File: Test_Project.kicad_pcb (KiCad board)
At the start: 4 copper layers, 72.5 x 56.2 mm, 72 parts, among them J1 Conn_01x02, J2 Conn_01x02, J3 Conn_01x03, J4 Conn_01x04, J5 Conn_01x04, J6 Conn_01x04, J7 Conn_01x04, Q1 NTTFS5C454NLTAG, Q2 NTTFS5C454NLTAG, Q3 NTTFS5C454NLTAG, Q4 NTTFS5C454NLTAG, Q5 BSS138-7-F, U1 STM32L081KZTx, U2 MIC2132YML, U3 AP2127N-3.3TRG1

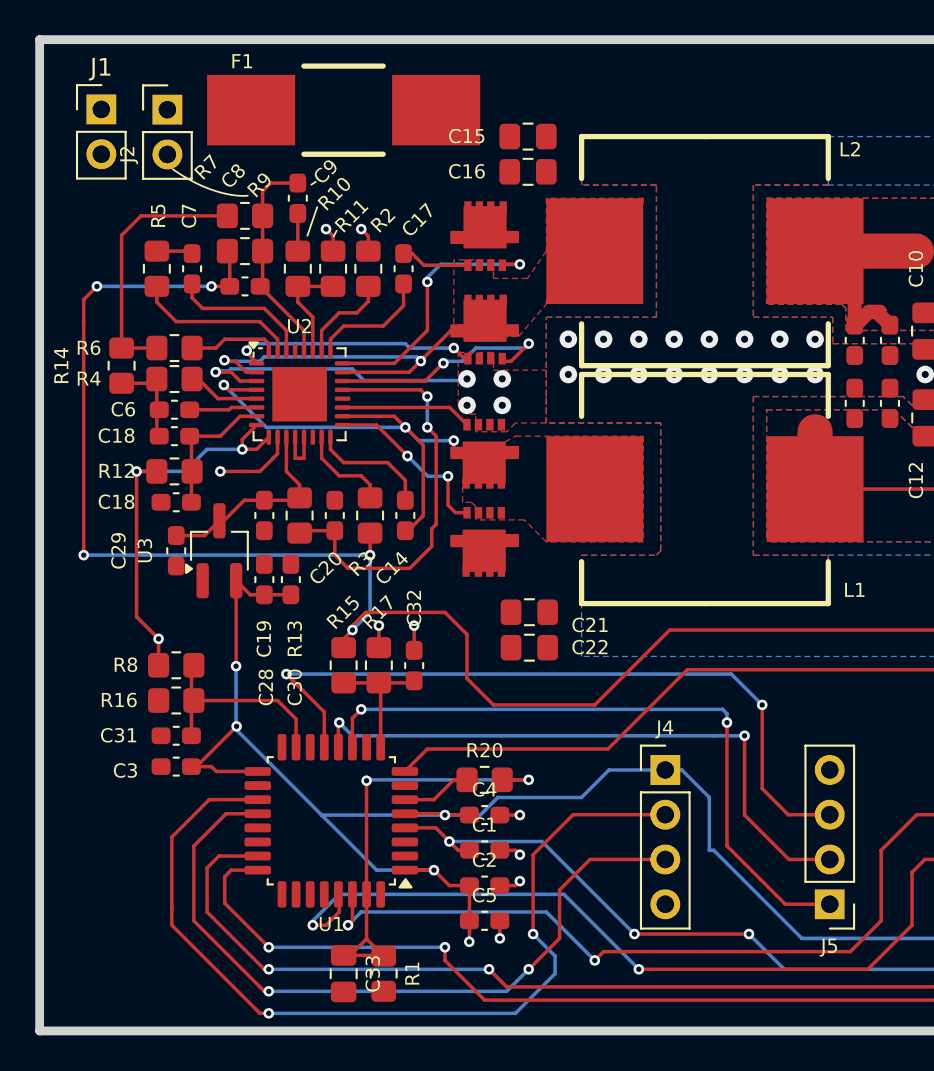
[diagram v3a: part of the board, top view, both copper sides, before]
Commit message: Finished up routing nets and pouring polygons. Needs final ground pours and review before ordering.
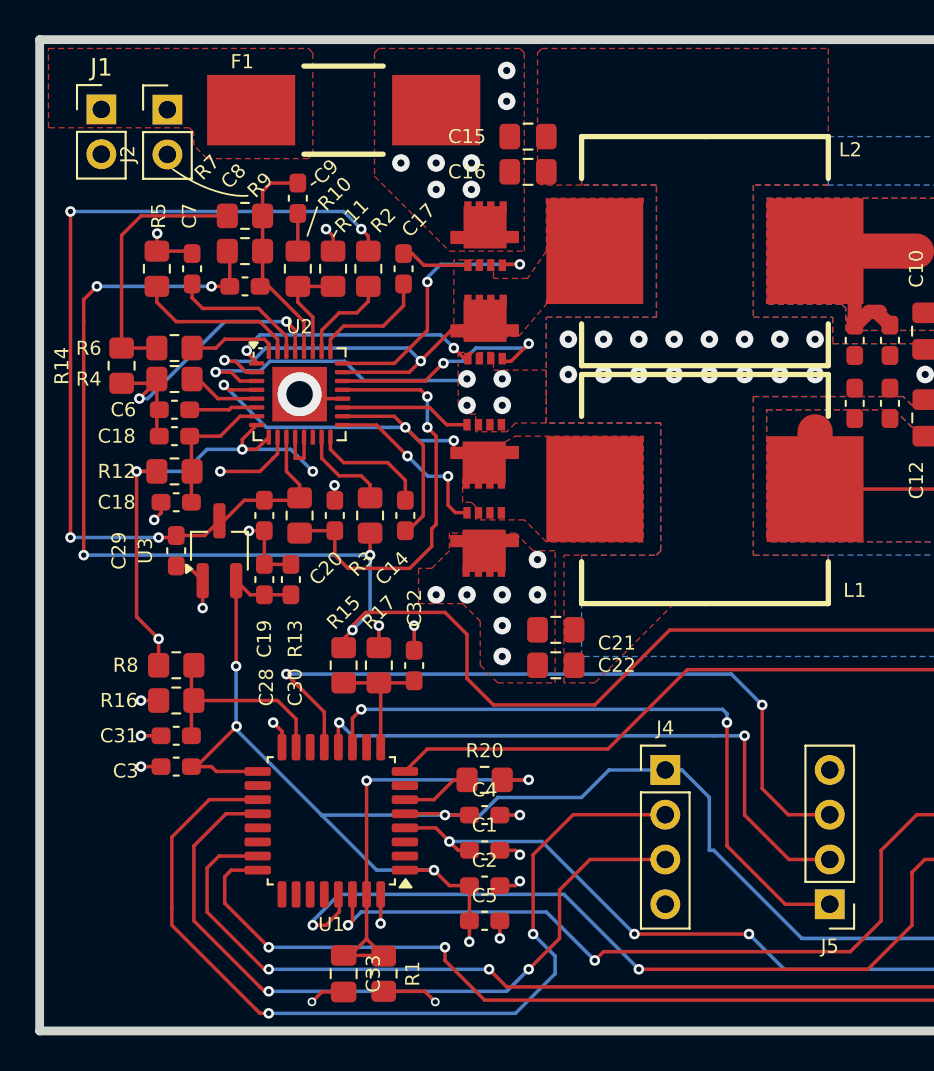
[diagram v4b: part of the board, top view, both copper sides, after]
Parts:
- moved C21 1.80 mm to (360.0, 104.5)
- moved C22 1.80 mm to (360.0, 106.5)
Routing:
- net GND: track 52.1 -> 100.3 mm, vias 33 -> 48
- net /VDD_5V: track 13.1 -> 54.5 mm, vias 1 -> 4
- net /Vin: track 22.7 -> 27.2 mm, vias 3 -> 18
- added copper zone on F.Cu, net /12V
- added copper zone on F.Cu, net /Vin
- added copper zone on In2.Cu, net /Vin
- added copper zone on In2.Cu, net /Vout

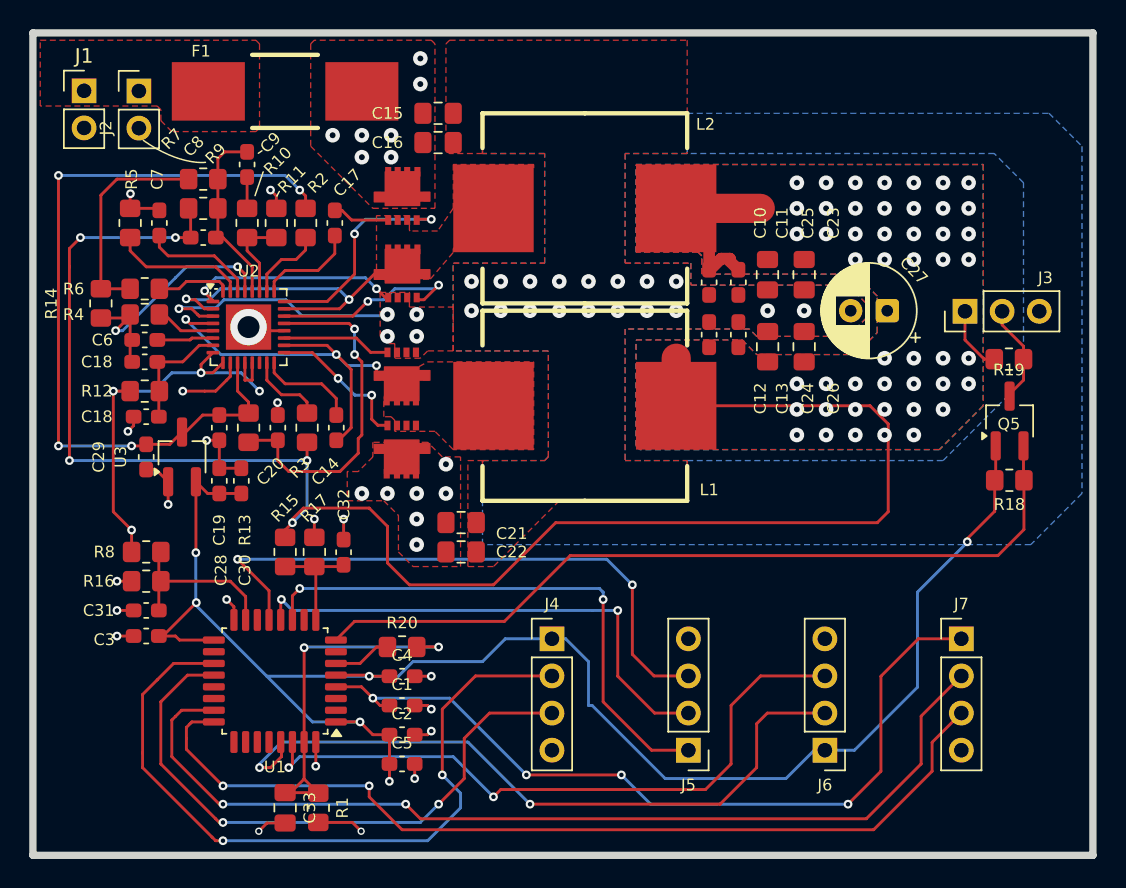
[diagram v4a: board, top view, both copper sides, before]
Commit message: Finished up layout and added some mounting holes.
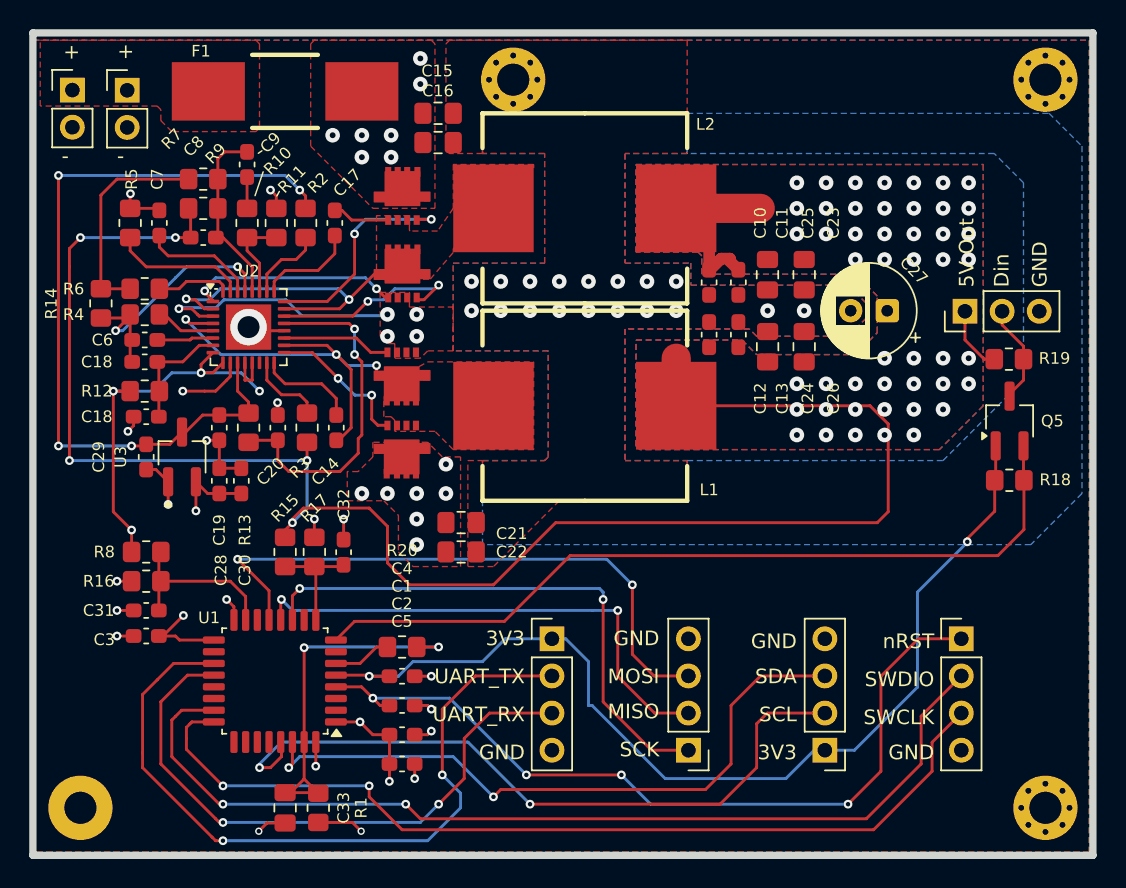
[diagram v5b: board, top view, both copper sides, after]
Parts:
- added ?: , Test_Project_Lib:, F.Cu at (334.0, 124.0)
- added ?: MountingHole_2.2mm_M2_Pad_Via, Test_Project_Lib:MountingHole_2.2mm_M2_Pad_Via, F.Cu at (363.6, 74.2)
- added ?: MountingHole_2.2mm_M2_Pad_Via, Test_Project_Lib:MountingHole_2.2mm_M2_Pad_Via, F.Cu at (400.0, 74.2)
- added ?: MountingHole_2.2mm_M2_Pad_Via, Test_Project_Lib:MountingHole_2.2mm_M2_Pad_Via, F.Cu at (400.0, 124.0)
- added G***: LOGO, Test_Project_Lib:LOGO, B.Cu at (369.6, 99.3)
- moved J1 0.80 mm to (333.4, 74.9)
- moved J2 0.80 mm to (337.2, 74.9)
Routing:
- net /VDD_3V3: track 117.3 -> 88.1 mm
- added copper zone on In2.Cu, net /12V
- added copper zone on In2.Cu, net /VDD_3V3
- added copper zone on In2.Cu, net /VDD_5V
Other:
- board text added: "+"
- board text added: "-"
- board text added: "3V3"
- board text added: "5V Out"
- board text added: "Din"
- board text added: "GND"
- board text added: "MISO"
- board text added: "MOSI"
- board text added: "SCK"
- board text added: "SCL"
- board text added: "SDA"
- board text added: "SWCLK"
- board text added: "SWDIO"
- board text added: "UART_RX"
- board text added: "UART_TX"
- board text added: "nRST"

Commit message: Daily commit. Working through test points and DRC checks.
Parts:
- removed the ? at (334.0, 124.0)
- added ?: , , F.Cu at (335.6, 125.0)
- added ?: , , F.Cu at (334.4, 125.5)
- added ?: , , F.Cu at (380.0, 97.2)
- added ?: , , F.Cu at (333.6, 86.8)
- added ?: , , F.Cu at (380.0, 82.0)
- added ?: , , F.Cu at (333.2, 125.0)
- added ?: , , F.Cu at (335.6, 122.6)
- added ?: , , F.Cu at (336.1, 123.8)
- added ?: , , F.Cu at (332.5, 84.1)
- added ?: , , F.Cu at (334.4, 122.2)
- added ?: , , F.Cu at (380.0, 102.2)
- added ?: , , F.Cu at (333.2, 122.6)
- added ?: , , F.Cu at (380.0, 77.0)
- added ?: , , F.Cu at (334.2, 123.8)
- added ?: , , F.Cu at (397.8, 83.8)
- added ?: , , F.Cu at (332.8, 123.8)
- C1: renamed from C7; footprint Test_Project_Lib:C_0603_1608Metric_Pad1.08x0.95mm_HandSolder -> Capacitor_SMD:C_0603_1608Metric_Pad1.08x0.95mm_HandSolder
- C10: renamed from C23; footprint Test_Project_Lib:C_0805_2012Metric_Pad1.18x1.45mm_HandSolder -> Capacitor_SMD:C_0805_2012Metric_Pad1.18x1.45mm_HandSolder
- C11: renamed from C6; footprint Test_Project_Lib:C_0603_1608Metric_Pad1.08x0.95mm_HandSolder -> Capacitor_SMD:C_0603_1608Metric_Pad1.08x0.95mm_HandSolder
- C12: renamed from C18; footprint Test_Project_Lib:C_0603_1608Metric_Pad1.08x0.95mm_HandSolder -> Capacitor_SMD:C_0603_1608Metric_Pad1.08x0.95mm_HandSolder
- C13: renamed from C29; footprint Test_Project_Lib:C_0603_1608Metric_Pad1.08x0.95mm_HandSolder -> Capacitor_SMD:C_0603_1608Metric_Pad1.08x0.95mm_HandSolder
- C14: renamed from C3; footprint Test_Project_Lib:C_0603_1608Metric_Pad1.08x0.95mm_HandSolder -> Capacitor_SMD:C_0603_1608Metric_Pad1.08x0.95mm_HandSolder
- C16: renamed from C31; footprint Test_Project_Lib:C_0603_1608Metric_Pad1.08x0.95mm_HandSolder -> Capacitor_SMD:C_0603_1608Metric_Pad1.08x0.95mm_HandSolder
- C17: renamed from C22; footprint Test_Project_Lib:C_0805_2012Metric_Pad1.18x1.45mm_HandSolder -> Capacitor_SMD:C_0805_2012Metric_Pad1.18x1.45mm_HandSolder
- C18: renamed from C21; footprint Test_Project_Lib:C_0805_2012Metric_Pad1.18x1.45mm_HandSolder -> Capacitor_SMD:C_0805_2012Metric_Pad1.18x1.45mm_HandSolder
- C19: renamed from C14; footprint Test_Project_Lib:C_0603_1608Metric_Pad1.08x0.95mm_HandSolder -> Capacitor_SMD:C_0603_1608Metric_Pad1.08x0.95mm_HandSolder
- C2: renamed from C8; footprint Test_Project_Lib:C_0603_1608Metric_Pad1.08x0.95mm_HandSolder -> Capacitor_SMD:C_0603_1608Metric_Pad1.08x0.95mm_HandSolder
- C20: footprint Test_Project_Lib:C_0603_1608Metric_Pad1.08x0.95mm_HandSolder -> Capacitor_SMD:C_0603_1608Metric_Pad1.08x0.95mm_HandSolder
- C21: renamed from C19; footprint Test_Project_Lib:C_0603_1608Metric_Pad1.08x0.95mm_HandSolder -> Capacitor_SMD:C_0603_1608Metric_Pad1.08x0.95mm_HandSolder
- C22: renamed from C30; footprint Test_Project_Lib:C_0603_1608Metric_Pad1.08x0.95mm_HandSolder -> Capacitor_SMD:C_0603_1608Metric_Pad1.08x0.95mm_HandSolder
- C23: renamed from C28; footprint Test_Project_Lib:C_0603_1608Metric_Pad1.08x0.95mm_HandSolder -> Capacitor_SMD:C_0603_1608Metric_Pad1.08x0.95mm_HandSolder
- C24: renamed from C32; footprint Test_Project_Lib:C_0603_1608Metric_Pad1.08x0.95mm_HandSolder -> Capacitor_SMD:C_0603_1608Metric_Pad1.08x0.95mm_HandSolder
- C25: renamed from C24; footprint Test_Project_Lib:C_0805_2012Metric_Pad1.18x1.45mm_HandSolder -> Capacitor_SMD:C_0805_2012Metric_Pad1.18x1.45mm_HandSolder
- C26: footprint Test_Project_Lib:C_0805_2012Metric_Pad1.18x1.45mm_HandSolder -> Capacitor_SMD:C_0805_2012Metric_Pad1.18x1.45mm_HandSolder
- C27: footprint Test_Project_Lib:CP_Radial_D6.3mm_P2.50mm -> Capacitor_THT:CP_Radial_D6.3mm_P2.50mm
- C28: renamed from C12; footprint Test_Project_Lib:C_0603_1608Metric_Pad1.08x0.95mm_HandSolder -> Capacitor_SMD:C_0603_1608Metric_Pad1.08x0.95mm_HandSolder
- C29: renamed from C13; footprint Test_Project_Lib:C_0603_1608Metric_Pad1.08x0.95mm_HandSolder -> Capacitor_SMD:C_0603_1608Metric_Pad1.08x0.95mm_HandSolder
- C3: renamed from C9; footprint Test_Project_Lib:C_0603_1608Metric_Pad1.08x0.95mm_HandSolder -> Capacitor_SMD:C_0603_1608Metric_Pad1.08x0.95mm_HandSolder
- C30: renamed from C2; footprint Test_Project_Lib:C_0603_1608Metric_Pad1.08x0.95mm_HandSolder -> Capacitor_SMD:C_0603_1608Metric_Pad1.08x0.95mm_HandSolder
- C31: renamed from C1; footprint Test_Project_Lib:C_0603_1608Metric_Pad1.08x0.95mm_HandSolder -> Capacitor_SMD:C_0603_1608Metric_Pad1.08x0.95mm_HandSolder
- C32: renamed from C4; footprint Test_Project_Lib:C_0603_1608Metric_Pad1.08x0.95mm_HandSolder -> Capacitor_SMD:C_0603_1608Metric_Pad1.08x0.95mm_HandSolder
- C33: renamed from C5; footprint Test_Project_Lib:C_0603_1608Metric_Pad1.08x0.95mm_HandSolder -> Capacitor_SMD:C_0603_1608Metric_Pad1.08x0.95mm_HandSolder
- C34: renamed from C33; footprint Test_Project_Lib:C_0805_2012Metric_Pad1.18x1.45mm_HandSolder -> Capacitor_SMD:C_0805_2012Metric_Pad1.18x1.45mm_HandSolder
- C4: renamed from C16; footprint Test_Project_Lib:C_0805_2012Metric_Pad1.18x1.45mm_HandSolder -> Capacitor_SMD:C_0805_2012Metric_Pad1.18x1.45mm_HandSolder
- C5: renamed from C15; footprint Test_Project_Lib:C_0805_2012Metric_Pad1.18x1.45mm_HandSolder -> Capacitor_SMD:C_0805_2012Metric_Pad1.18x1.45mm_HandSolder
- C6: renamed from C17; footprint Test_Project_Lib:C_0603_1608Metric_Pad1.08x0.95mm_HandSolder -> Capacitor_SMD:C_0603_1608Metric_Pad1.08x0.95mm_HandSolder
- C7: renamed from C25; footprint Test_Project_Lib:C_0805_2012Metric_Pad1.18x1.45mm_HandSolder -> Capacitor_SMD:C_0805_2012Metric_Pad1.18x1.45mm_HandSolder
- C8: renamed from C11; footprint Test_Project_Lib:C_0603_1608Metric_Pad1.08x0.95mm_HandSolder -> Capacitor_SMD:C_0603_1608Metric_Pad1.08x0.95mm_HandSolder
- C9: renamed from C10; footprint Test_Project_Lib:C_0603_1608Metric_Pad1.08x0.95mm_HandSolder -> Capacitor_SMD:C_0603_1608Metric_Pad1.08x0.95mm_HandSolder
- J1: renamed from J2; footprint Test_Project_Lib:PinHeader_1x02_P2.54mm_Vertical -> Connector_PinHeader_2.54mm:PinHeader_1x02_P2.54mm_Vertical
- J2: renamed from J1; footprint Test_Project_Lib:PinHeader_1x02_P2.54mm_Vertical -> Connector_PinHeader_2.54mm:PinHeader_1x02_P2.54mm_Vertical
- J3: renamed from J4; footprint Test_Project_Lib:PinHeader_1x04_P2.54mm_Vertical -> Connector_PinHeader_2.54mm:PinHeader_1x04_P2.54mm_Vertical
- J4: renamed from J7; footprint Test_Project_Lib:PinHeader_1x04_P2.54mm_Vertical -> Connector_PinHeader_2.54mm:PinHeader_1x04_P2.54mm_Vertical
- J5: renamed from J3; footprint Test_Project_Lib:PinHeader_1x03_P2.54mm_Vertical -> Connector_PinHeader_2.54mm:PinHeader_1x03_P2.54mm_Vertical
- J6: renamed from J5; footprint Test_Project_Lib:PinHeader_1x04_P2.54mm_Vertical -> Connector_PinHeader_2.54mm:PinHeader_1x04_P2.54mm_Vertical
- J7: renamed from J6; footprint Test_Project_Lib:PinHeader_1x04_P2.54mm_Vertical -> Connector_PinHeader_2.54mm:PinHeader_1x04_P2.54mm_Vertical
- R1: renamed from R7; value 3.3k -> 3.3kΩ; footprint Test_Project_Lib:R_0805_2012Metric_Pad1.20x1.40mm_HandSolder -> Resistor_SMD:R_0805_2012Metric_Pad1.20x1.40mm_HandSolder
- R10: renamed from R12; value 100k -> 100kΩ; footprint Test_Project_Lib:R_0805_2012Metric_Pad1.20x1.40mm_HandSolder -> Resistor_SMD:R_0805_2012Metric_Pad1.20x1.40mm_HandSolder
- R11: renamed from R16; value 10k -> 10kΩ; footprint Test_Project_Lib:R_0805_2012Metric_Pad1.20x1.40mm_HandSolder -> Resistor_SMD:R_0805_2012Metric_Pad1.20x1.40mm_HandSolder
- R12: renamed from R14; value 3.3k -> 3.3kΩ; footprint Test_Project_Lib:R_0805_2012Metric_Pad1.20x1.40mm_HandSolder -> Resistor_SMD:R_0805_2012Metric_Pad1.20x1.40mm_HandSolder
- R13: renamed from R17; value 10k -> 10kΩ; footprint Test_Project_Lib:R_0805_2012Metric_Pad1.20x1.40mm_HandSolder -> Resistor_SMD:R_0805_2012Metric_Pad1.20x1.40mm_HandSolder
- R14: renamed from R15; footprint Test_Project_Lib:R_0805_2012Metric_Pad1.20x1.40mm_HandSolder -> Resistor_SMD:R_0805_2012Metric_Pad1.20x1.40mm_HandSolder
- R15: renamed from R13; footprint Test_Project_Lib:R_0805_2012Metric_Pad1.20x1.40mm_HandSolder -> Resistor_SMD:R_0805_2012Metric_Pad1.20x1.40mm_HandSolder
- R16: renamed from R3; value 10k -> 10kΩ; footprint Test_Project_Lib:R_0805_2012Metric_Pad1.20x1.40mm_HandSolder -> Resistor_SMD:R_0805_2012Metric_Pad1.20x1.40mm_HandSolder
- R17: renamed from R20; value 3.3k -> 3.3kΩ; footprint Test_Project_Lib:R_0805_2012Metric_Pad1.20x1.40mm_HandSolder -> Resistor_SMD:R_0805_2012Metric_Pad1.20x1.40mm_HandSolder
- R18, R19: footprint Test_Project_Lib:R_0805_2012Metric_Pad1.20x1.40mm_HandSolder -> Resistor_SMD:R_0805_2012Metric_Pad1.20x1.40mm_HandSolder
- R2: renamed from R9; footprint Test_Project_Lib:R_0805_2012Metric_Pad1.20x1.40mm_HandSolder -> Resistor_SMD:R_0805_2012Metric_Pad1.20x1.40mm_HandSolder
- R20: renamed from R1; footprint Test_Project_Lib:R_0805_2012Metric_Pad1.20x1.40mm_HandSolder -> Resistor_SMD:R_0805_2012Metric_Pad1.20x1.40mm_HandSolder
- R3: renamed from R5; footprint Test_Project_Lib:R_0805_2012Metric_Pad1.20x1.40mm_HandSolder -> Resistor_SMD:R_0805_2012Metric_Pad1.20x1.40mm_HandSolder
- R4: renamed from R6; value 100k -> 100kΩ; footprint Test_Project_Lib:R_0805_2012Metric_Pad1.20x1.40mm_HandSolder -> Resistor_SMD:R_0805_2012Metric_Pad1.20x1.40mm_HandSolder
- R5: renamed from R2; value 10k -> 10kΩ; footprint Test_Project_Lib:R_0805_2012Metric_Pad1.20x1.40mm_HandSolder -> Resistor_SMD:R_0805_2012Metric_Pad1.20x1.40mm_HandSolder
- R6: renamed from R10; value 100k -> 100kΩ; footprint Test_Project_Lib:R_0805_2012Metric_Pad1.20x1.40mm_HandSolder -> Resistor_SMD:R_0805_2012Metric_Pad1.20x1.40mm_HandSolder
- R7: renamed from R11; value 100k -> 100kΩ; footprint Test_Project_Lib:R_0805_2012Metric_Pad1.20x1.40mm_HandSolder -> Resistor_SMD:R_0805_2012Metric_Pad1.20x1.40mm_HandSolder
- R8: renamed from R4; footprint Test_Project_Lib:R_0805_2012Metric_Pad1.20x1.40mm_HandSolder -> Resistor_SMD:R_0805_2012Metric_Pad1.20x1.40mm_HandSolder
- R9: renamed from R8; value 100k -> 100kΩ; footprint Test_Project_Lib:R_0805_2012Metric_Pad1.20x1.40mm_HandSolder -> Resistor_SMD:R_0805_2012Metric_Pad1.20x1.40mm_HandSolder
- U1: renamed from U3; footprint Test_Project_Lib:SOT-23W_Handsoldering -> Package_TO_SOT_SMD:SOT-23W_Handsoldering
- U2: footprint Test_Project_Lib:QFN-32-1EP_5x5mm_P0.5mm_EP3.1x3.1mm -> Package_DFN_QFN:QFN-32-1EP_5x5mm_P0.5mm_EP3.1x3.1mm
- U3: renamed from U1; value STM32L081KZTx -> STM32L081KZT6; footprint Test_Project_Lib:LQFP-32_7x7mm_P0.8mm -> Package_QFP:LQFP-32_7x7mm_P0.8mm
- renumbered C18 to C15, L2 to L1, L1 to L2, Q3 to Q1, Q4 to Q2, Q2 to Q3, Q1 to Q4
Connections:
- C12 pad 1: Net-(U2-EN) -> Net-(U3-EN)
- R10 pad 1: Net-(U2-EN) -> Net-(U3-EN)
- R5 pad 1: /VDD_5V -> Net-(U3-PG)
- R5 pad 2: Net-(U2-PG) -> /VDD_5V
- U2 pad 26: Net-(U2-PG) -> Net-(U3-PG)
- U2 pad 7: Net-(U2-EN) -> Net-(U3-EN)
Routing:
- net Net-(J3-Pin_2): track 0.00 -> 13.4 mm
- net Net-(J7-Pin_2): track 6.80 -> 0.00 mm
- net /Vout: track 137.9 -> 141.9 mm
- net GND: vias 48 -> 47
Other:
- board text added: "5V"
- board text added: "Vout"

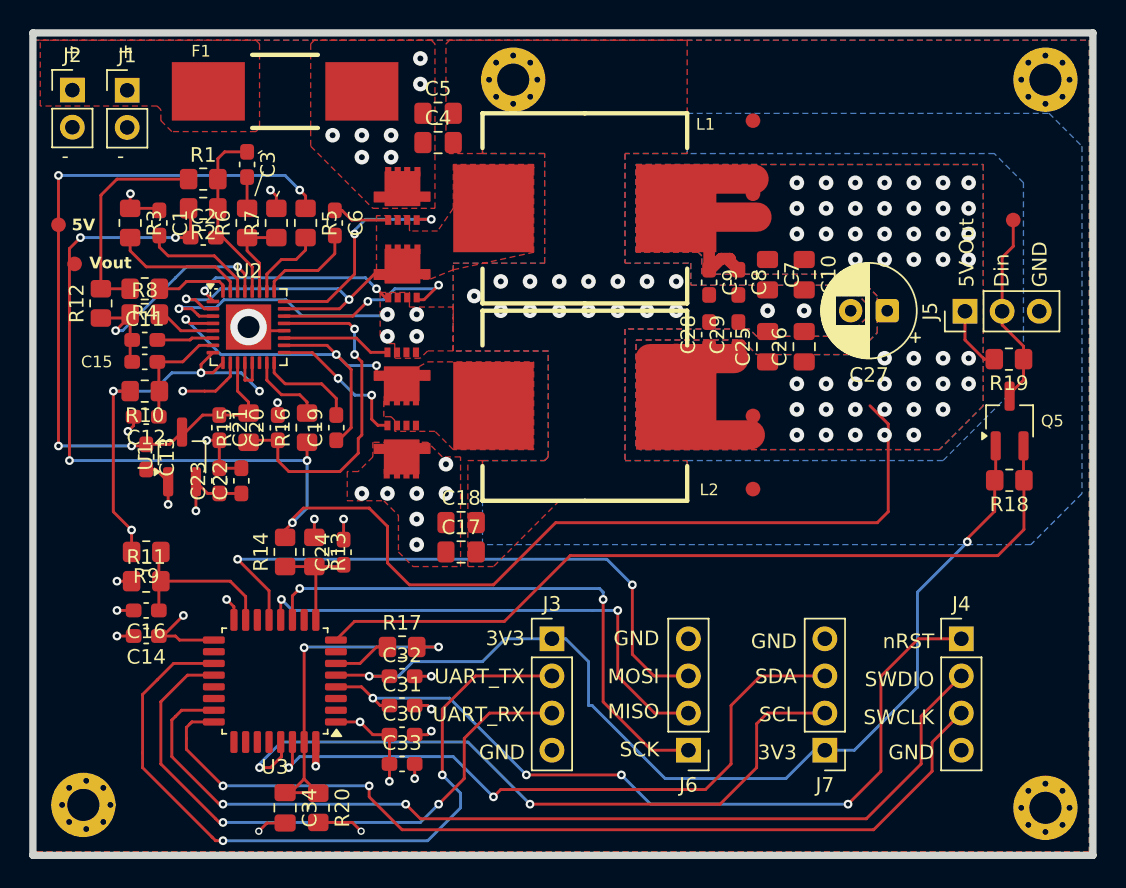
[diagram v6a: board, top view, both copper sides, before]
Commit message: Modified footprints, redid silkscreen designators to be geographical on PCB rather than on schematic (experimental) Started process of DRC. Will need to check against JLC's requirements (should be good)
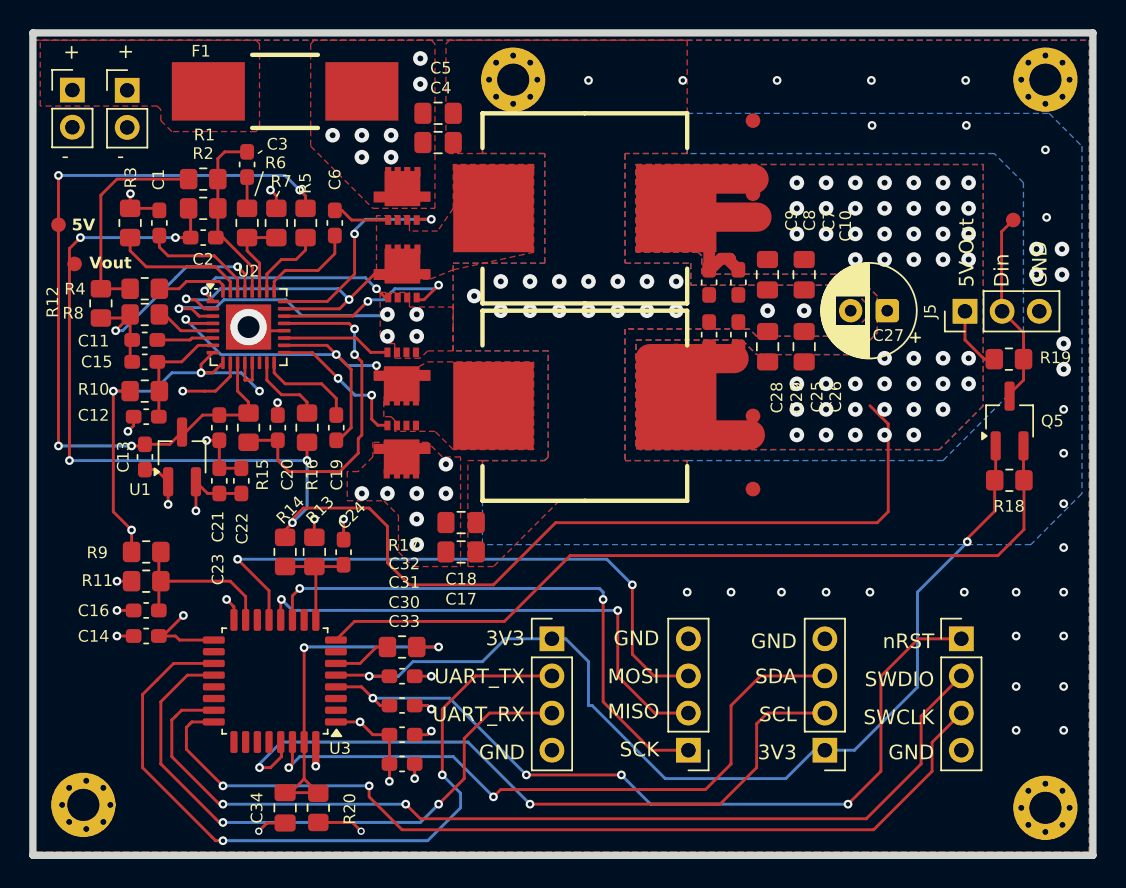
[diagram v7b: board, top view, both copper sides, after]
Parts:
- R1, R10, R11, R12, R13, R14, R15, R16, R17, R18, R19, R2, R20, R3, R4, R5, R6, R7, R8, R9: footprint Resistor_SMD:R_0805_2012Metric_Pad1.20x1.40mm_HandSolder -> Test_Project_Lib:R_0805_2012Metric_Pad1.20x1.40mm_HandSolder
- moved C13 0.09 mm to (338.4, 100.0)
- turned R5 to 90 degrees
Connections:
- ? pad 1: Net-(J3-Pin_2) -> Net-(J7-Pin_2)
- C15 pad 1: Net-(U2-EN) -> Net-(U3-EN)
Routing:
- net Net-(J7-Pin_2): track 0.00 -> 13.4 mm
- net Net-(J3-Pin_2): track 13.4 -> 0.00 mm
- net Net-(U3-EN): track 0.00 -> 8.06 mm
- net Net-(U2-EN): track 8.06 -> 0.00 mm
- net Net-(U3-PG): track 0.00 -> 5.37 mm
- net Net-(U2-PG): track 5.37 -> 0.00 mm
- net GND: vias 47 -> 80

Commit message: Updated footprint 3d models in local library.
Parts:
- ? (x16): footprint (none) -> Test_Project_Lib:
- C1, C11, C12, C13, C14, C16, C19, C2, C20, C21, C22, C23, C24, C28, C29, C3, C30, C31, C32, C33, C6, C8, C9: footprint Capacitor_SMD:C_0603_1608Metric_Pad1.08x0.95mm_HandSolder -> Test_Project_Lib:C_0603_1608Metric_Pad1.08x0.95mm_HandSolder
- C10, C17, C18, C25, C26, C34, C4, C5, C7: footprint Capacitor_SMD:C_0805_2012Metric_Pad1.18x1.45mm_HandSolder -> Test_Project_Lib:C_0805_2012Metric_Pad1.18x1.45mm_HandSolder
- C27: footprint Capacitor_THT:CP_Radial_D6.3mm_P2.50mm -> Test_Project_Lib:CP_Radial_D6.3mm_P2.50mm
- J1, J2: footprint Connector_PinHeader_2.54mm:PinHeader_1x02_P2.54mm_Vertical -> Test_Project_Lib:PinHeader_1x02_P2.54mm_Vertical
- J3, J4, J6, J7: footprint Connector_PinHeader_2.54mm:PinHeader_1x04_P2.54mm_Vertical -> Test_Project_Lib:PinHeader_1x04_P2.54mm_Vertical
- J5: footprint Connector_PinHeader_2.54mm:PinHeader_1x03_P2.54mm_Vertical -> Test_Project_Lib:PinHeader_1x03_P2.54mm_Vertical
- U1: footprint Package_TO_SOT_SMD:SOT-23W_Handsoldering -> Test_Project_Lib:SOT-23W_Handsoldering
- U2: footprint Package_DFN_QFN:QFN-32-1EP_5x5mm_P0.5mm_EP3.1x3.1mm -> Test_Project_Lib:QFN-32-1EP_5x5mm_P0.5mm_EP3.1x3.1mm
- U3: footprint Package_QFP:LQFP-32_7x7mm_P0.8mm -> Test_Project_Lib:LQFP-32_7x7mm_P0.8mm
